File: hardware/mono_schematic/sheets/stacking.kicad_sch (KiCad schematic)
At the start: 16 parts

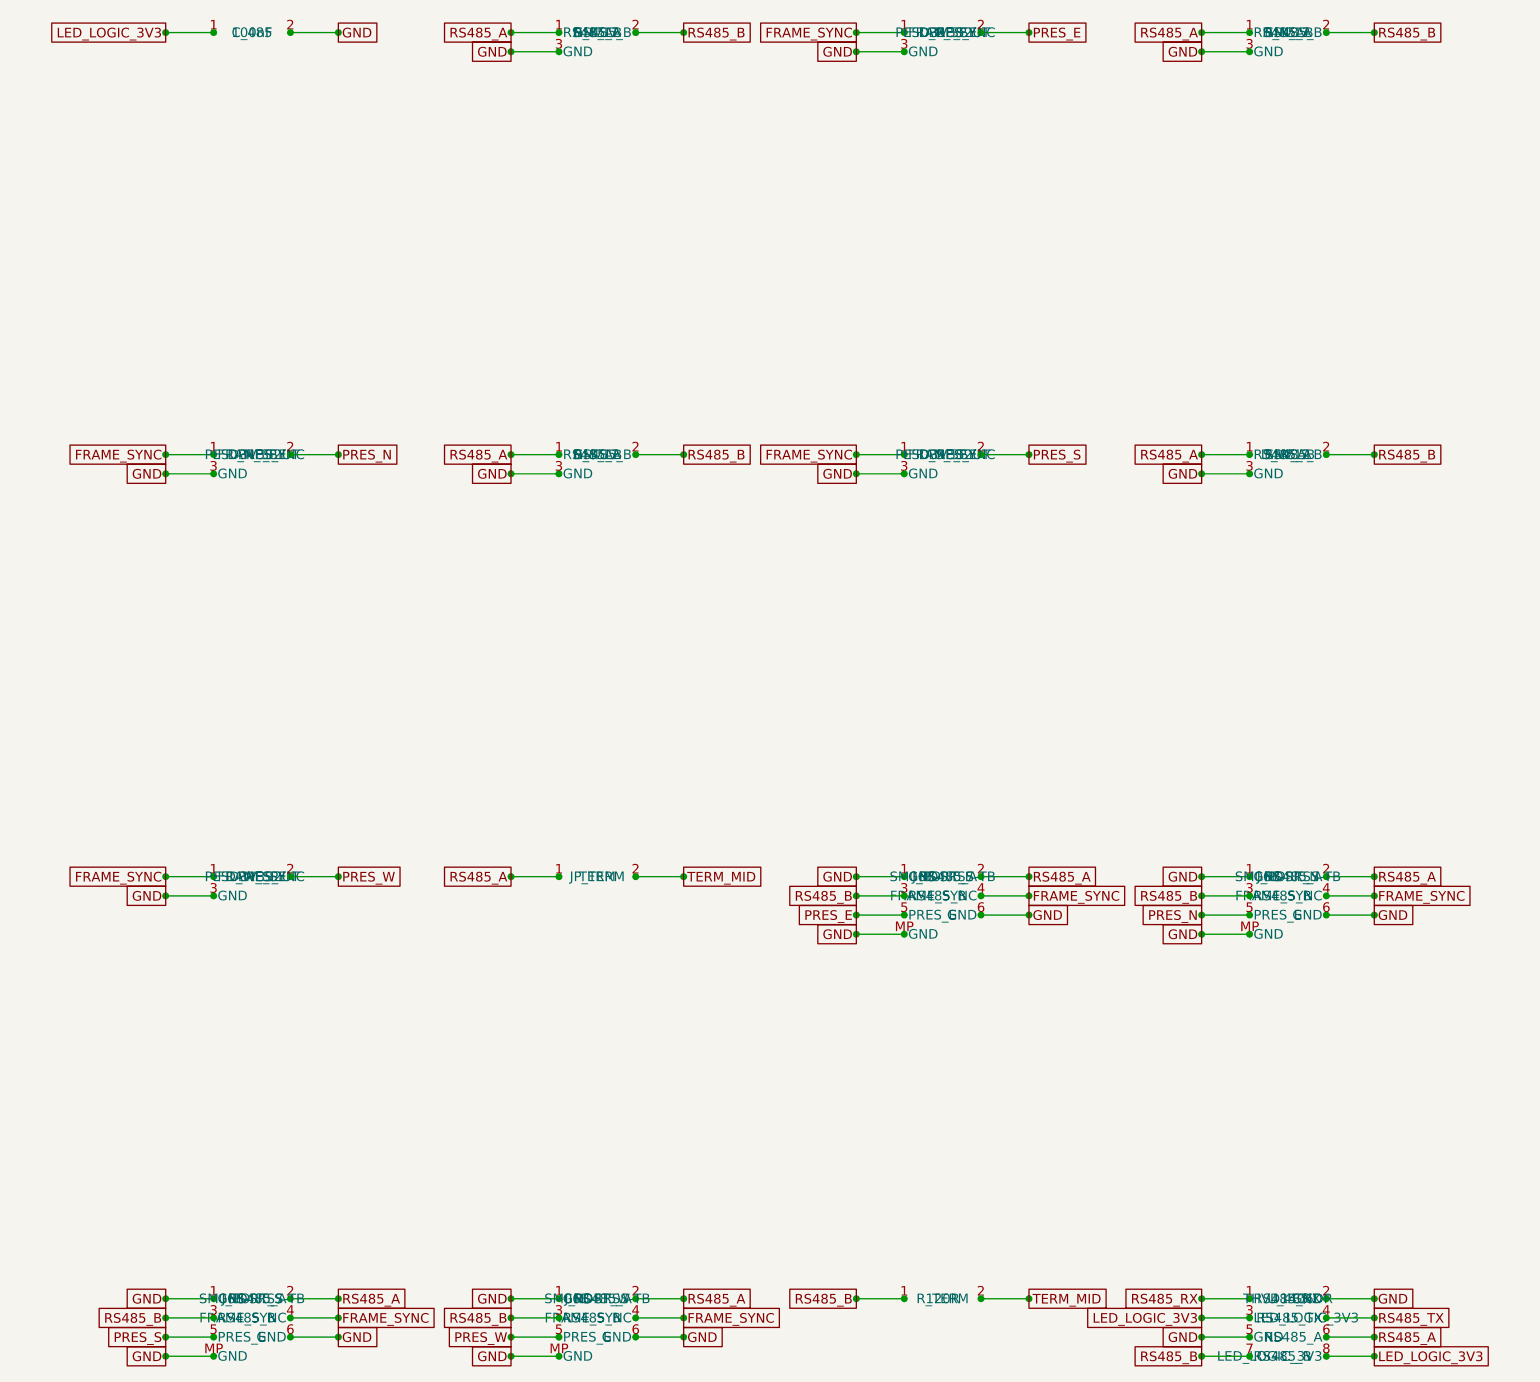
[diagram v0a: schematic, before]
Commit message: mono_electronics v11b: TLV75733P 1A AON LDO, 22uF ESP32 bulk, LED_EN RC glitch filter, J_USB value, refs end in digit; schematic regenerated (ERC 0, 0 diffs)
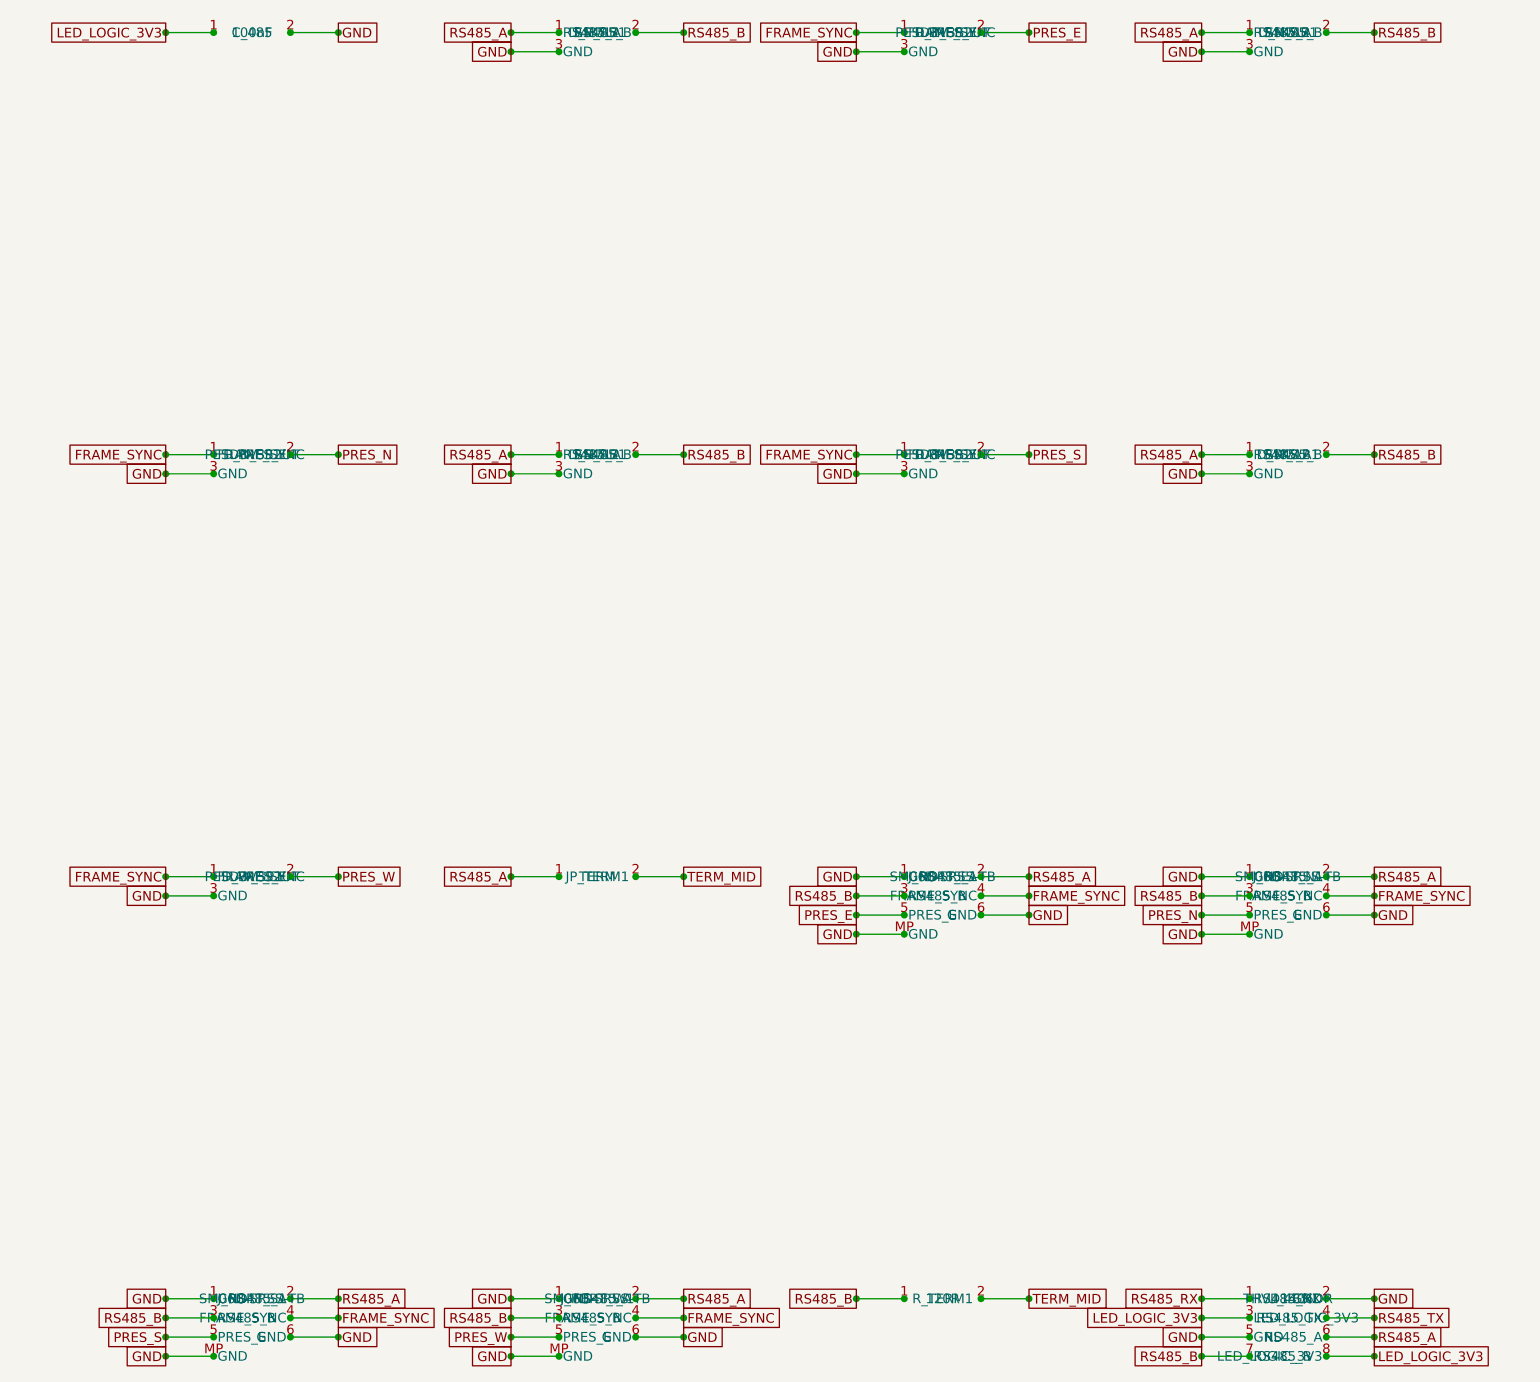
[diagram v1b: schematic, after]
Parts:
- removed D_E_AB, D_N_AB, D_S_AB, D_W_AB: SM712, mono_electronics:SOT-23, symbol mono_parts:SM712_SOT-23_3
- removed D_E_SP, D_N_SP, D_S_SP, D_W_SP: PESD3V3S2UT, mono_electronics:SOT-23, symbol mono_parts:PESD3V3S2UT_SOT-23_3
- removed JP_TERM: TERM, mono_electronics:SolderJumper-2_P1.3mm_Open_RoundedPad1.0x1.5mm, symbol mono_parts:TERM_SolderJumper-2_P1.3mm_Open_RoundedPad1.0x1.5mm_2
- removed J_PORT_E, J_PORT_N, J_PORT_S, J_PORT_W: SM06B-SRSS-TB, mono_electronics:JST_SH_SM06B-SRSS-TB_1x06-1MP_P1.00mm_Horizontal, symbol mono_parts:SM06B-SRSS-TB_JST_SH_SM06B-SRSS-TB_1x06-1MP_P1.00mm_Horizontal_7
- removed R_TERM: 120R, mono_electronics:R_0603_1608Metric, symbol mono_parts:120R_R_0603_1608Metric_2
- added D_E_AB1, D_N_AB1, D_S_AB1, D_W_AB1: SM712, mono_electronics:SOT-23, symbol mono_parts:SM712_SOT-23_3
- added D_E_SP1, D_N_SP1, D_S_SP1, D_W_SP1: PESD3V3S2UT, mono_electronics:SOT-23, symbol mono_parts:PESD3V3S2UT_SOT-23_3
- added JP_TERM1: TERM, mono_electronics:SolderJumper-2_P1.3mm_Open_RoundedPad1.0x1.5mm, symbol mono_parts:TERM_SolderJumper-2_P1.3mm_Open_RoundedPad1.0x1.5mm_2
- added J_PORT_E1, J_PORT_N1, J_PORT_S1, J_PORT_W1: SM06B-SRSS-TB, mono_electronics:JST_SH_SM06B-SRSS-TB_1x06-1MP_P1.00mm_Horizontal, symbol mono_parts:SM06B-SRSS-TB_JST_SH_SM06B-SRSS-TB_1x06-1MP_P1.00mm_Horizontal_7
- added R_TERM1: 120R, mono_electronics:R_0603_1608Metric, symbol mono_parts:120R_R_0603_1608Metric_2
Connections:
- net FRAME_SYNC: now also D_E_SP1.1 (FRAME_SYNC), D_N_SP1.1 (FRAME_SYNC), D_S_SP1.1 (FRAME_SYNC), D_W_SP1.1 (FRAME_SYNC), J_PORT_E1.4 (FRAME_SYNC), J_PORT_N1.4 (FRAME_SYNC), J_PORT_S1.4 (FRAME_SYNC), J_PORT_W1.4 (FRAME_SYNC)
- net GND: now also D_E_AB1.3 (GND), D_E_SP1.3 (GND), D_N_AB1.3 (GND), D_N_SP1.3 (GND), D_S_AB1.3 (GND), D_S_SP1.3 (GND), D_W_AB1.3 (GND), D_W_SP1.3 (GND), J_PORT_E1.1 (GND), J_PORT_E1.6 (GND), J_PORT_E1.MP (GND), J_PORT_N1.1 (GND), J_PORT_N1.6 (GND), J_PORT_N1.MP (GND), J_PORT_S1.1 (GND), J_PORT_S1.6 (GND), J_PORT_S1.MP (GND), J_PORT_W1.1 (GND), J_PORT_W1.6 (GND), J_PORT_W1.MP (GND)
- net PRES_E: now also D_E_SP1.2 (PRES_E), J_PORT_E1.5 (PRES_E)
- net PRES_N: now also D_N_SP1.2 (PRES_E), J_PORT_N1.5 (PRES_E)
- net PRES_S: now also D_S_SP1.2 (PRES_E), J_PORT_S1.5 (PRES_E)
- net PRES_W: now also D_W_SP1.2 (PRES_E), J_PORT_W1.5 (PRES_E)
- net RS485_A: now also D_E_AB1.1 (RS485_A), D_N_AB1.1 (RS485_A), D_S_AB1.1 (RS485_A), D_W_AB1.1 (RS485_A), JP_TERM1.1, J_PORT_E1.2 (RS485_A), J_PORT_N1.2 (RS485_A), J_PORT_S1.2 (RS485_A), J_PORT_W1.2 (RS485_A)
- net RS485_B: now also D_E_AB1.2 (RS485_B), D_N_AB1.2 (RS485_B), D_S_AB1.2 (RS485_B), D_W_AB1.2 (RS485_B), J_PORT_E1.3 (RS485_B), J_PORT_N1.3 (RS485_B), J_PORT_S1.3 (RS485_B), J_PORT_W1.3 (RS485_B), R_TERM1.1
- net TERM_MID: now also JP_TERM1.2, R_TERM1.2
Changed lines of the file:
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@@
     (instances
       (project "mono_electronics"
-        (path "/fcdb2d07-c4a6-4633-9c7a-2d69fa84f395"
+        (path "/cd156f04-e4a8-43b2-8f0f-334815ded034"
           (reference "C_485")
           (unit 1)
@@
     (property
       "Reference"
-      "D_E_AB"
+      "D_E_AB1"
       (at 81.28 35.56 0)
       (effects
@@
     (instances
       (project "mono_electronics"
-        (path "/fcdb2d07-c4a6-4633-9c7a-2d69fa84f395"
-          (reference "D_E_AB")
+        (path "/cd156f04-e4a8-43b2-8f0f-334815ded034"
+          (reference "D_E_AB1")
           (unit 1)
         )
@@
     (property
       "Reference"
-      "D_E_SP"
+      "D_E_SP1"
       (at 127 35.56 0)
       (effects
@@
     (instances
       (project "mono_electronics"
-        (path "/fcdb2d07-c4a6-4633-9c7a-2d69fa84f395"
-          (reference "D_E_SP")
+        (path "/cd156f04-e4a8-43b2-8f0f-334815ded034"
+          (reference "D_E_SP1")
           (unit 1)
         )
@@
     (property
       "Reference"
-      "D_N_AB"
+      "D_N_AB1"
       (at 172.72 35.56 0)
       (effects
@@
     (instances
       (project "mono_electronics"
-        (path "/fcdb2d07-c4a6-4633-9c7a-2d69fa84f395"
-          (reference "D_N_AB")
+        (path "/cd156f04-e4a8-43b2-8f0f-334815ded034"
+          (reference "D_N_AB1")
           (unit 1)
         )
@@
     (property
       "Reference"
-      "D_N_SP"
+      "D_N_SP1"
       (at 35.56 91.44 0)
       (effects
@@
     (instances
       (project "mono_electronics"
-        (path "/fcdb2d07-c4a6-4633-9c7a-2d69fa84f395"
-          (reference "D_N_SP")
+        (path "/cd156f04-e4a8-43b2-8f0f-334815ded034"
+          (reference "D_N_SP1")
           (unit 1)
         )
@@
     (property
       "Reference"
-      "D_S_AB"
+      "D_S_AB1"
       (at 81.28 91.44 0)
       (effects
@@
     (instances
       (project "mono_electronics"
-        (path "/fcdb2d07-c4a6-4633-9c7a-2d69fa84f395"
-          (reference "D_S_AB")
+        (path "/cd156f04-e4a8-43b2-8f0f-334815ded034"
+          (reference "D_S_AB1")
           (unit 1)
         )
@@
     (property
       "Reference"
-      "D_S_SP"
+      "D_S_SP1"
       (at 127 91.44 0)
       (effects
@@
     (instances
       (project "mono_electronics"
-        (path "/fcdb2d07-c4a6-4633-9c7a-2d69fa84f395"
-          (reference "D_S_SP")
+        (path "/cd156f04-e4a8-43b2-8f0f-334815ded034"
+          (reference "D_S_SP1")
           (unit 1)
         )
@@
     (property
       "Reference"
-      "D_W_AB"
+      "D_W_AB1"
       (at 172.72 91.44 0)
       (effects
@@
     (instances
       (project "mono_electronics"
-        (path "/fcdb2d07-c4a6-4633-9c7a-2d69fa84f395"
-          (reference "D_W_AB")
+        (path "/cd156f04-e4a8-43b2-8f0f-334815ded034"
+          (reference "D_W_AB1")
           (unit 1)
         )
@@
     (property
       "Reference"
-      "D_W_SP"
+      "D_W_SP1"
       (at 35.56 147.32 0)
       (effects
@@
     (instances
       (project "mono_electronics"
-        (path "/fcdb2d07-c4a6-4633-9c7a-2d69fa84f395"
-          (reference "D_W_SP")
+        (path "/cd156f04-e4a8-43b2-8f0f-334815ded034"
+          (reference "D_W_SP1")
           (unit 1)
         )
@@
     (property
       "Reference"
-      "JP_TERM"
+      "JP_TERM1"
       (at 81.28 147.32 0)
       (effects
@@
     (instances
       (project "mono_electronics"
-        (path "/fcdb2d07-c4a6-4633-9c7a-2d69fa84f395"
-          (reference "JP_TERM")
+        (path "/cd156f04-e4a8-43b2-8f0f-334815ded034"
+          (reference "JP_TERM1")
           (unit 1)
         )
@@
     (property
       "Reference"
-      "J_PORT_E"
+      "J_PORT_E1"
       (at 127 147.32 0)
       (effects
@@
     (instances
       (project "mono_electronics"
-        (path "/fcdb2d07-c4a6-4633-9c7a-2d69fa84f395"
-          (reference "J_PORT_E")
+        (path "/cd156f04-e4a8-43b2-8f0f-334815ded034"
+          (reference "J_PORT_E1")
           (unit 1)
         )
@@
     (property
       "Reference"
-      "J_PORT_N"
+      "J_PORT_N1"
       (at 172.72 147.32 0)
       (effects
@@
     (instances
       (project "mono_electronics"
-        (path "/fcdb2d07-c4a6-4633-9c7a-2d69fa84f395"
-          (reference "J_PORT_N")
+        (path "/cd156f04-e4a8-43b2-8f0f-334815ded034"
+          (reference "J_PORT_N1")
           (unit 1)
         )
@@
     (property
       "Reference"
-      "J_PORT_S"
+      "J_PORT_S1"
       (at 35.56 203.2 0)
       (effects
@@
     (instances
       (project "mono_electronics"
-        (path "/fcdb2d07-c4a6-4633-9c7a-2d69fa84f395"
-          (reference "J_PORT_S")
+        (path "/cd156f04-e4a8-43b2-8f0f-334815ded034"
+          (reference "J_PORT_S1")
           (unit 1)
         )
@@
     (property
       "Reference"
-      "J_PORT_W"
+      "J_PORT_W1"
       (at 81.28 203.2 0)
       (effects
@@
     (instances
       (project "mono_electronics"
-        (path "/fcdb2d07-c4a6-4633-9c7a-2d69fa84f395"
-          (reference "J_PORT_W")
+        (path "/cd156f04-e4a8-43b2-8f0f-334815ded034"
+          (reference "J_PORT_W1")
           (unit 1)
         )
@@
     (property
       "Reference"
-      "R_TERM"
+      "R_TERM1"
       (at 127 203.2 0)
       (effects
@@
     (instances
       (project "mono_electronics"
-        (path "/fcdb2d07-c4a6-4633-9c7a-2d69fa84f395"
-          (reference "R_TERM")
+        (path "/cd156f04-e4a8-43b2-8f0f-334815ded034"
+          (reference "R_TERM1")
           (unit 1)
         )
@@
     (instances
       (project "mono_electronics"
-        (path "/fcdb2d07-c4a6-4633-9c7a-2d69fa84f395"
+        (path "/cd156f04-e4a8-43b2-8f0f-334815ded034"
           (reference "U_485")
           (unit 1)
@@
   )
   (sheet_instances
-    (path "/fcdb2d07-c4a6-4633-9c7a-2d69fa84f395"
+    (path "/cd156f04-e4a8-43b2-8f0f-334815ded034"
       (page "1")
     )
